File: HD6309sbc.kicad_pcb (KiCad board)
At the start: 2 copper layers, 99.8 x 99.8 mm, 28 parts, among them J1 Conn_01x02_Male, J2 Conn_02x30_Odd_Even, J3 Conn_01x02_Male, U1 HD63C09, U10 74HC375, U11 74HC02, U12 74HC21, U13 74HC21, U15 74AHC1G08, U2 74HC163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

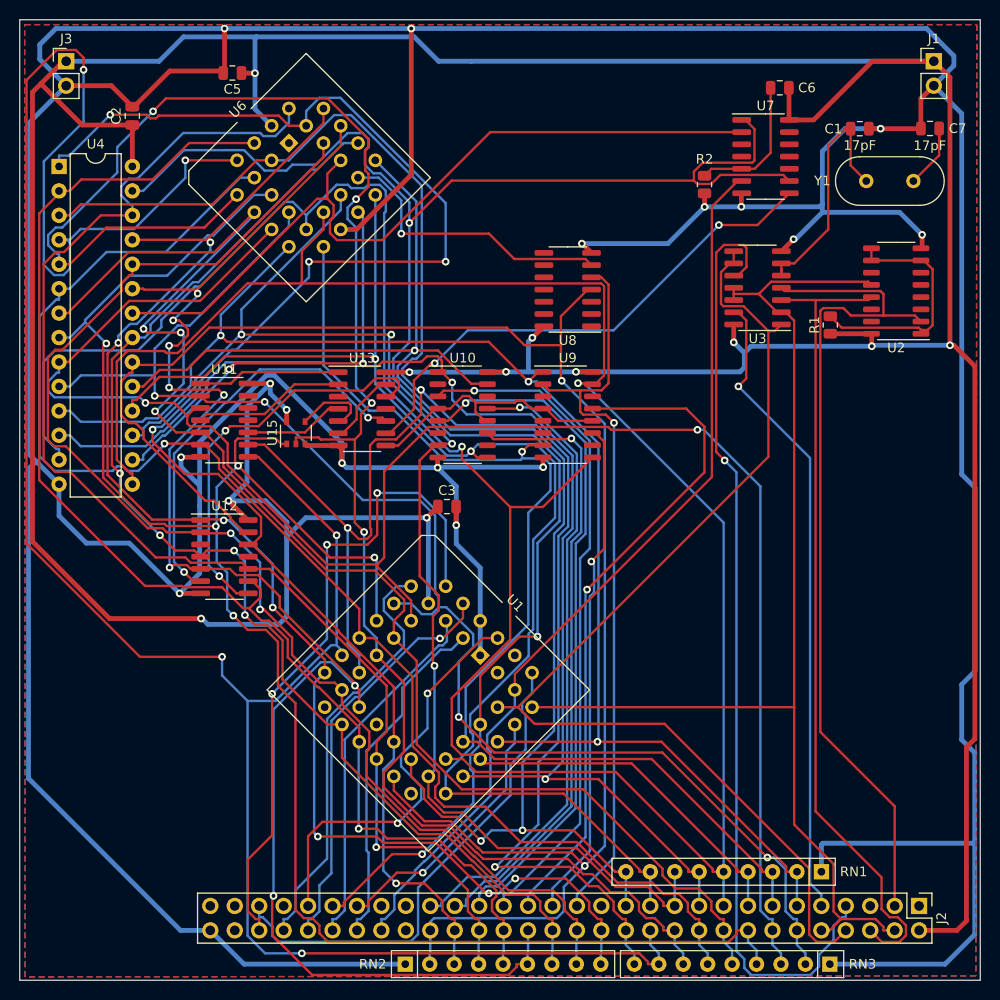
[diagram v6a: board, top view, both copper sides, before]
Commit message: modify address logic for mapped registers
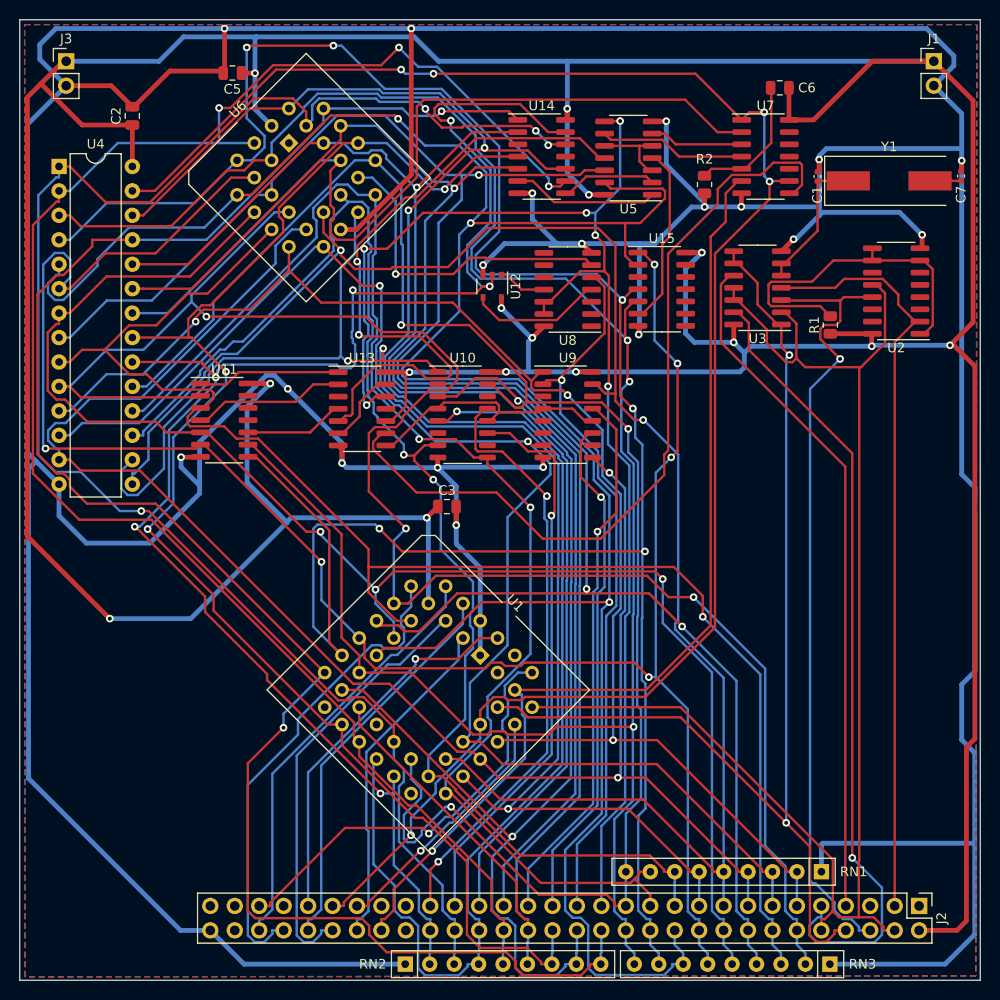
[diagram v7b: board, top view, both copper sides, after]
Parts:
- added U14: 74HC21D, Package_SO:SOIC-14_3.9x8.7mm_P1.27mm, F.Cu at (79.6, 39.6)
- added U5: 74HC08, Package_SO:SOIC-14_3.9x8.7mm_P1.27mm, F.Cu at (88.7, 39.8)
- C1, C7: footprint Capacitor_SMD:C_0805_2012Metric -> Capacitor_SMD:C_0402_1005Metric
- C3: value 1uF -> 100uF
- R2: value R -> 2.2K
- U10, U9: value 74HC375 -> 74LS375D
- U12: value 74HC21 -> 74AHC1G08; footprint Package_SO:SO-14_3.9x8.65mm_P1.27mm -> Package_SO:TSOP-5_1.65x3.05mm_P0.95mm
- U13: value 74HC21 -> 74HC21D; footprint Package_SO:SO-14_3.9x8.65mm_P1.27mm -> Package_SO:SOIC-14_3.9x8.7mm_P1.27mm
- U15: value 74AHC1G08 -> 74HC21D; footprint Package_SO:TSOP-5_1.65x3.05mm_P0.95mm -> Package_SO:SOIC-14_3.9x8.7mm_P1.27mm
- U2: footprint Package_SO:SO-16_3.9x9.9mm_P1.27mm -> Package_SO:SOIC-16_3.9x9.9mm_P1.27mm
- U3: value 74HC02 -> 74HC02D; footprint Package_SO:SO-14_3.9x8.65mm_P1.27mm -> Package_SO:SOIC-14_3.9x8.7mm_P1.27mm
- U7: value 74HC04 -> 74HC04D; footprint Package_SO:SO-14_3.9x8.65mm_P1.27mm -> Package_SO:SOIC-14_3.9x8.7mm_P1.27mm
- U8: value 74HC00 -> 74HC00D; footprint Package_SO:SO-14_3.9x8.65mm_P1.27mm -> Package_SO:SOIC-14_3.9x8.7mm_P1.27mm
- Y1: footprint Crystal:Crystal_HC18-U_Vertical -> Crystal:Crystal_SMD_HC49-SD
- moved U15 40.8 mm to (92.1, 53.4), turned to 0 degrees
- moved U12 39.5 mm to (74.5, 53.1), turned to -90 degrees
- moved C1 6.63 mm to (108.3, 41.7), turned to 90 degrees
- moved C7 5.90 mm to (123.2, 41.6), turned to 90 degrees
- moved Y1 2.38 mm to (115.8, 42.1)
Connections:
- J2 pad 27: unconnected-(J2-Pad27) -> MAPPED_MEM
- U12 pad 1: A8 -> Net-(U8-Pad11)
- U12 pad 2: A9 -> A15
- U12 pad 3: (no net) -> GND
- U12 pad 4: A10 -> Net-(U8-Pad4)
- U12 pad 5: A11 -> +5V
- U13 pad 10: Net-(U12-Pad6) -> +5V
- U13 pad 12: Net-(U12-Pad8) -> MAPPED_MEM
- U15 pad 1: A2 -> A4
- U15 pad 3: GND -> (no net)
- U15 pad 4: Net-(U13-Pad5) -> A6
- U15 pad 5: +5V -> A7
- U7 pad 3: (no net) -> Vector
- U7 pad 4: (no net) -> Net-(U7-Pad4)
- U8 pad 11: unconnected-(U8-Pad11) -> Net-(U8-Pad11)
- U8 pad 12: unconnected-(U8-Pad12) -> MAPPED_MEM
- U8 pad 13: unconnected-(U8-Pad13) -> MAPPED_MEM
- U8 pad 4: A15 -> Net-(U8-Pad4)
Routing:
- net MAPPED_MEM: track 0.00 -> 140.6 mm, vias 0 -> 6
- net Net-(U13-Pad5): track 8.15 -> 69.1 mm, vias 0 -> 2
- net A4: track 149.0 -> 208.3 mm, vias 1 -> 6
- net A13: track 139.6 -> 194.6 mm, vias 1 -> 2
- net A5: track 188.8 -> 240.6 mm, vias 4 -> 3
- net A9: track 137.2 -> 186.3 mm
- net Net-(U12-Pad8): track 42.8 -> 0.00 mm, vias 2 -> 0
- net Net-(U12-Pad6): track 42.7 -> 0.00 mm, vias 2 -> 0
- net A8: track 147.6 -> 189.0 mm, vias 7 -> 2
- net A12: track 138.6 -> 178.3 mm, vias 1 -> 3
- net A0: track 150.8 -> 186.8 mm, vias 4 -> 3
- net Net-(U13-Pad9): track 54.0 -> 85.1 mm, vias 2 -> 0
- net A1: track 188.3 -> 157.9 mm, vias 2 -> 1
- net +5V: track 464.6 -> 494.8 mm, vias 13 -> 15
- net ~{E}: track 98.9 -> 71.7 mm, vias 1 -> 0
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- added copper zone on B.Cu, net GND
- added copper zone on F.Cu, net GND
- removed copper zone on B.Cu, net (none)
- removed copper zone on F.Cu, net (none)
